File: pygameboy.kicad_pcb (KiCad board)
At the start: 2 copper layers, 49.3 x 59.7 mm, 93 parts, among them J1 Conn_01x01, J2 Conn_01x01, J3 Conn_ARM_JTAG_SWD_10, J4 USB_B_Micro, J5 MIDI IN, J6 MIDI OUT, Q1 BSS138, SW1 SW_Push, U1 CARTRIDGE, U2 SAMD51J, U3 74LVC244, U4 74LVC244, U5 74x4245, U6 74LVC244, U7 AP2204K-3.3, U8 H11L1

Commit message: Final v5 version
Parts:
- removed the G*** at (140.4, 46.0)
- added FID0: TestPoint, Fiducial:Fiducial_1mm_Mask2mm, F.Cu at (138.9, 82.5)
- added FID1: TestPoint, Fiducial:Fiducial_1mm_Mask2mm, F.Cu at (101.9, 55.0)
- added G***: LOGO, chickadee:chickadee_1mm_ss, F.Cu at (121.3, 44.9)
- added G***: Chickadee 3mm, chickadee:chickadee_3mm_fcu, B.Cu at (115.1, 45.8)
- added TP48: Test_Point, TestPoint:TestPoint_Pad_D1.5mm, B.Cu at (101.4, 95.5)
- added TP49: Test_Point, TestPoint:TestPoint_Pad_D1.5mm, B.Cu at (102.9, 92.5)
- added TP50: Test_Point, TestPoint:TestPoint_Pad_D1.5mm, B.Cu at (104.4, 95.5)
- added TP51: Test_Point, TestPoint:TestPoint_Pad_D1.5mm, B.Cu at (105.9, 92.5)
- added TP52: Test_Point, TestPoint:TestPoint_Pad_D1.5mm, B.Cu at (107.4, 95.5)
- added TP53: Test_Point, TestPoint:TestPoint_Pad_D1.5mm, B.Cu at (108.9, 92.5)
- added TP54: Test_Point, TestPoint:TestPoint_Pad_D1.5mm, B.Cu at (110.4, 95.5)
- added TP55: Test_Point, TestPoint:TestPoint_Pad_D1.5mm, B.Cu at (111.9, 92.5)
- added TP56: Test_Point, TestPoint:TestPoint_Pad_D1.5mm, B.Cu at (113.4, 95.5)
- added TP57: Test_Point, TestPoint:TestPoint_Pad_D1.5mm, B.Cu at (114.9, 92.5)
- added TP58: Test_Point, TestPoint:TestPoint_Pad_D1.5mm, B.Cu at (116.4, 95.5)
- added TP59: Test_Point, TestPoint:TestPoint_Pad_D1.5mm, B.Cu at (117.9, 92.5)
- added TP60: Test_Point, TestPoint:TestPoint_Pad_D1.5mm, B.Cu at (119.4, 95.5)
- added TP61: Test_Point, TestPoint:TestPoint_Pad_D1.5mm, B.Cu at (120.9, 92.5)
- added TP62: Test_Point, TestPoint:TestPoint_Pad_D1.5mm, B.Cu at (122.4, 95.5)
- added TP63: Test_Point, TestPoint:TestPoint_Pad_D1.5mm, B.Cu at (123.9, 92.5)
- added TP64: Test_Point, TestPoint:TestPoint_Pad_D1.5mm, B.Cu at (125.4, 95.5)
- added TP65: Test_Point, TestPoint:TestPoint_Pad_D1.5mm, B.Cu at (126.9, 92.5)
- added TP66: Test_Point, TestPoint:TestPoint_Pad_D1.5mm, B.Cu at (128.4, 95.5)
- added TP67: Test_Point, TestPoint:TestPoint_Pad_D1.5mm, B.Cu at (129.9, 92.5)
- added TP68: Test_Point, TestPoint:TestPoint_Pad_D1.5mm, B.Cu at (131.4, 95.5)
- added TP69: Test_Point, TestPoint:TestPoint_Pad_D1.5mm, B.Cu at (132.9, 92.5)
- added TP70: Test_Point, TestPoint:TestPoint_Pad_D1.5mm, B.Cu at (134.4, 95.5)
- added TP71: Test_Point, TestPoint:TestPoint_Pad_D1.5mm, B.Cu at (135.9, 92.5)
- added TP72: Test_Point, TestPoint:TestPoint_Pad_D1.5mm, B.Cu at (137.4, 95.5)
- added TP73: Test_Point, TestPoint:TestPoint_Pad_D1.5mm, B.Cu at (138.9, 92.5)
- added TP74: Test_Point, TestPoint:TestPoint_Pad_D1.5mm, B.Cu at (140.4, 95.5)
- added TP75: Test_Point, TestPoint:TestPoint_Pad_D1.5mm, B.Cu at (141.9, 92.5)
- added TP76: Test_Point, TestPoint:TestPoint_Pad_D1.5mm, B.Cu at (143.4, 95.4)
- added TP77: Test_Point, TestPoint:TestPoint_Pad_D1.5mm, B.Cu at (144.9, 92.5)
- added TP78: Test_Point, TestPoint:TestPoint_Pad_D1.5mm, B.Cu at (146.4, 95.5)
- added TP79: Test_Point, TestPoint:TestPoint_Pad_D1.5mm, B.Cu at (147.9, 92.5)
- added TP80: Test_Point, TestPoint:TestPoint_Pad_D1.5mm, B.Cu at (136.9, 43.0)
- added TP81: Test_Point, TestPoint:TestPoint_Pad_D1.5mm, B.Cu at (138.4, 45.5)
- added TP82: Test_Point, TestPoint:TestPoint_Pad_D1.5mm, B.Cu at (141.4, 45.5)
- added TP83: Test_Point, TestPoint:TestPoint_Pad_D1.5mm, B.Cu at (135.4, 45.5)
- added TP84: Test_Point, TestPoint:TestPoint_Pad_D1.5mm, B.Cu at (139.9, 43.0)
- added TP85: Test_Point, TestPoint:TestPoint_Pad_D1.5mm, B.Cu at (138.4, 41.0)
- moved R1 1.67 mm to (120.7, 50.5), turned to 270 degrees
- moved TP37 0.90 mm to (145.9, 50.2)
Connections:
- net Net-(TP31-Pad1) renamed /AUD
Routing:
- net /AUD: track 9.02 -> 19.0 mm
- net +BATT: track 19.0 -> 27.3 mm
- net /CS: track 13.8 -> 21.6 mm
- net /WR: track 16.9 -> 24.7 mm
- net /D5: track 45.1 -> 52.8 mm
- net /D3: track 44.4 -> 52.1 mm
- net /D1: track 45.2 -> 53.0 mm
- net /A7: track 18.1 -> 25.9 mm
- net /A5: track 14.4 -> 22.2 mm
- net /A3: track 12.6 -> 20.4 mm
- net /A15: track 13.1 -> 20.8 mm
- net /A11: track 17.6 -> 25.3 mm
- net /A1: track 17.0 -> 24.8 mm
- net /A9: track 12.6 -> 20.4 mm
- net /A13: track 13.9 -> 21.7 mm
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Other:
- outline, holes or cut-outs redrawn
- board text added: "+3V"
- board text added: "SWCLK"
- board text added: "SWDIO"
- board text added: "SWO"

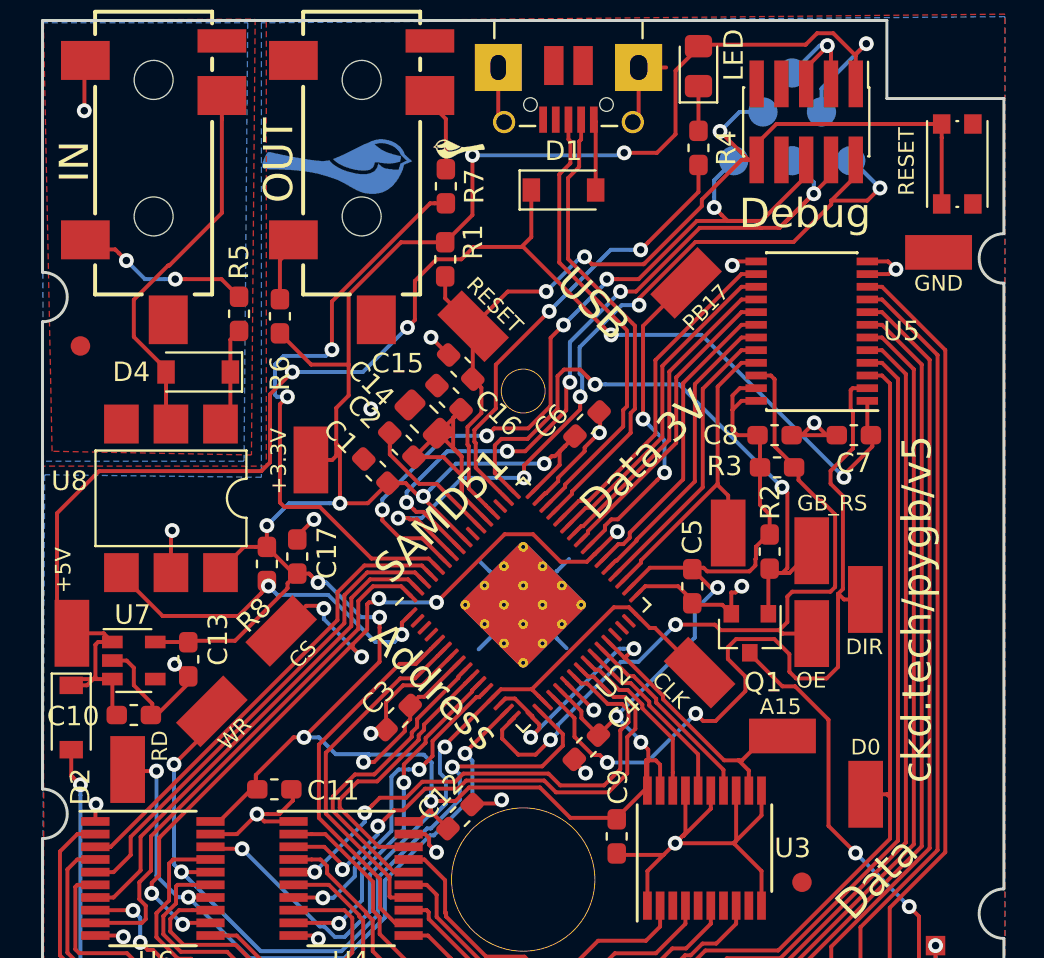
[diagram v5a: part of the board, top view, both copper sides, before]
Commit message: Correct optoistolator footprint. Tweak spacing.
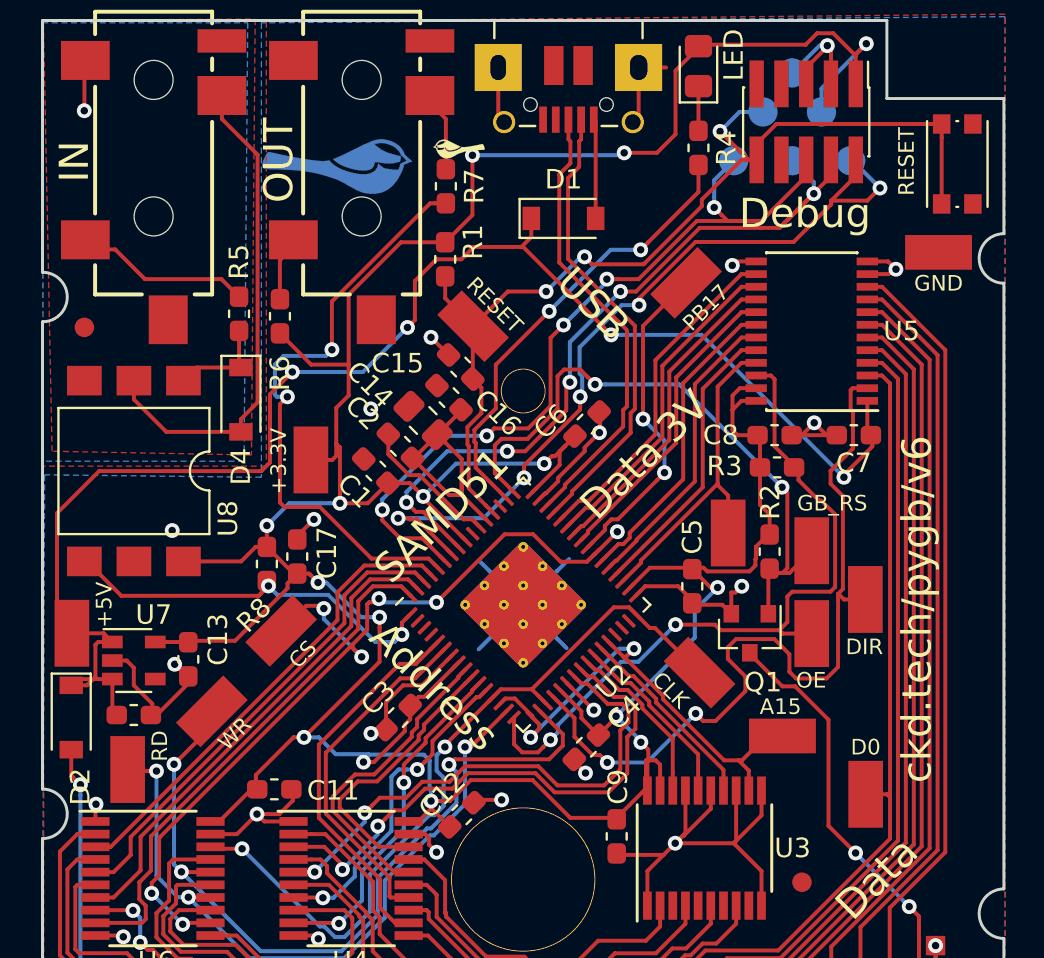
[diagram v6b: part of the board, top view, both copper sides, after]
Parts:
- TP33, TP34, TP35, TP36, TP37, TP38, TP39, TP40, TP41, TP42, TP43, TP44, TP45, TP46, TP47: footprint keystone:5015-SMT-TestPoint -> keystone:5015-SMT-TestPoint-NoPaste
- U8: footprint Package_DIP:SMDIP-6_W7.62mm -> Package_DIP:SMDIP-6_W9.53mm
- moved D4 2.61 mm to (110.2, 57.7), turned to 270 degrees
- moved U8 2.36 mm to (104.7, 61.4)
- moved D1 1.46 mm to (126.7, 48.4)
- moved FID1 0.97 mm to (102.1, 54.0)
- moved C12 0.13 mm to (121.5, 79.0)
- moved C2 0.10 mm to (118.4, 60.1)
- moved C14 0.09 mm to (119.5, 58.8)
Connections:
- J1 pad 1: Net-(J1-Pad1) -> (no net)
- J2 pad 1: Net-(J2-Pad1) -> (no net)
- J3 pad 7: Net-(J3-Pad7) -> (no net)
- J3 pad 8: Net-(J3-Pad8) -> (no net)
- J3 pad 9: Net-(J3-Pad9) -> (no net)
- J4 pad 4: Net-(J4-Pad4) -> (no net)
- J5 pad RN: Net-(J5-PadRN) -> (no net)
- J5 pad TN: Net-(J5-PadTN) -> (no net)
- J6 pad RN: Net-(J6-PadRN) -> (no net)
- J6 pad TN: Net-(J6-PadTN) -> (no net)
- U2 pad 2: Net-(U2-Pad2) -> (no net)
- U2 pad 29: Net-(U2-Pad29) -> (no net)
- U2 pad 3: Net-(U2-Pad3) -> (no net)
- U2 pad 30: Net-(U2-Pad30) -> (no net)
- U2 pad 31: Net-(U2-Pad31) -> (no net)
- U2 pad 4: Net-(U2-Pad4) -> (no net)
- U2 pad 51: Net-(U2-Pad51) -> (no net)
- U2 pad 55: Net-(U2-Pad55) -> (no net)
- U3 pad 3: Net-(U3-Pad3) -> (no net)
- U3 pad 5: Net-(U3-Pad5) -> (no net)
- U3 pad 7: Net-(U3-Pad7) -> (no net)
- U3 pad 9: Net-(U3-Pad9) -> (no net)
- U7 pad 4: Net-(U7-Pad4) -> (no net)
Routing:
- net Net-(D4-Pad2): track 19.5 -> 25.5 mm
- net Net-(C14-Pad2): track 15.6 -> 13.4 mm
- net GND: track 144.0 -> 142.1 mm
- net +3V3: track 196.0 -> 197.8 mm
- net +5V: track 78.8 -> 77.4 mm
- net VBUS: track 3.65 -> 5.10 mm
- net /MIDI_IN: track 18.6 -> 19.8 mm
- net /DATA_OE: track 38.5 -> 37.7 mm
- net Net-(J5-PadT): vias 2 -> 0
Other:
- board text added: "ckd.tech/pygb/v6"
- board text removed: "ckd.tech/pygb/v5"

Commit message: rp2040 start
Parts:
- removed G***: LOGO, chickadee:chickadee_1mm_ss
- removed G***: Chickadee 3mm, chickadee:chickadee_3mm_fcu
- removed TP38: 3.3v, keystone:5015-SMT-TestPoint-NoPaste
- removed TP44: PB17, keystone:5015-SMT-TestPoint-NoPaste
- added C18: 0.1uF, Capacitor_SMD:C_0603_1608Metric_Pad1.08x0.95mm_HandSolder, F.Cu at (118.4, 69.2)
- added C19: 1uF, Capacitor_SMD:C_0603_1608Metric_Pad1.08x0.95mm_HandSolder, F.Cu at (87.2, 45.6)
- added C20: 0.1uF, Capacitor_SMD:C_0603_1608Metric_Pad1.08x0.95mm_HandSolder, F.Cu at (91.5, 43.0)
- added C21: 0.1uF, Capacitor_SMD:C_0603_1608Metric_Pad1.08x0.95mm_HandSolder, F.Cu at (95.9, 40.5)
- added C22: 0.1uF, Capacitor_SMD:C_0603_1608Metric_Pad1.08x0.95mm_HandSolder, F.Cu at (126.9, 75.0)
- added R10: 1k, Resistor_SMD:R_0603_1608Metric_Pad0.98x0.95mm_HandSolder, F.Cu at (122.7, 76.2)
- added R11: 27, Resistor_SMD:R_0603_1608Metric_Pad0.98x0.95mm_HandSolder, F.Cu at (127.5, 59.5)
- added R12: 27, Resistor_SMD:R_0603_1608Metric_Pad0.98x0.95mm_HandSolder, F.Cu at (128.0, 61.5)
- added R9: 10k, Resistor_SMD:R_0603_1608Metric_Pad0.98x0.95mm_HandSolder, F.Cu at (118.3, 60.3)
- added U9: W25Q32JVSS, Package_SO:SOIC-8_5.23x5.23mm_P1.27mm, F.Cu at (118.4, 59.4)
- added Y1: 12mhz, Crystal:Crystal_SMD_Abracon_ABM3C-4Pin_5.0x3.2mm, F.Cu at (124.1, 77.6)
- C1, C2: value 0.1uF -> 22pF; footprint Capacitor_SMD:C_0603_1608Metric_Pad1.05x0.95mm_HandSolder -> Capacitor_SMD:C_0402_1005Metric_Pad0.74x0.62mm_HandSolder
- C10, C11, C12, C13, C16, C17, C3, C5, C6, C7, C8, C9: footprint Capacitor_SMD:C_0603_1608Metric_Pad1.05x0.95mm_HandSolder -> Capacitor_SMD:C_0603_1608Metric_Pad1.08x0.95mm_HandSolder
- C14: value 10uF -> 0.1uF; footprint Capacitor_SMD:C_0805_2012Metric_Pad1.15x1.40mm_HandSolder -> Capacitor_SMD:C_0603_1608Metric_Pad1.08x0.95mm_HandSolder
- C15: value 1uF -> 0.1uF; footprint Capacitor_SMD:C_0603_1608Metric_Pad1.05x0.95mm_HandSolder -> Capacitor_SMD:C_0603_1608Metric_Pad1.08x0.95mm_HandSolder
- C4: value 0.1uF -> 1uF; footprint Capacitor_SMD:C_0603_1608Metric_Pad1.05x0.95mm_HandSolder -> Capacitor_SMD:C_0603_1608Metric_Pad1.08x0.95mm_HandSolder
- R1, R2, R3, R4, R5, R6, R7, R8: footprint Resistor_SMD:R_0603_1608Metric_Pad1.05x0.95mm_HandSolder -> Resistor_SMD:R_0603_1608Metric_Pad0.98x0.95mm_HandSolder
- TP33, TP34, TP35, TP36, TP37, TP39, TP40, TP41, TP42, TP43, TP45, TP46, TP47: footprint keystone:5015-SMT-TestPoint-NoPaste -> keystone:5015-SMT-TestPoint
- U2: value SAMD51J -> RP2040; footprint Package_DFN_QFN:QFN-64-1EP_9x9mm_P0.5mm_EP4.7x4.7mm_ThermalVias -> MCU_RaspberryPi_and_Boards:RP2040-QFN-56
- moved C15 33.9 mm to (91.5, 40.5), turned to 0 degrees
- moved TP36 31.7 mm to (153.3, 48.3)
- moved C2 23.9 mm to (128.5, 81.7), turned to 0 degrees
- moved C1 21.9 mm to (125.3, 81.7), turned to 0 degrees
- moved C14 15.1 mm to (130.6, 69.1), turned to 0 degrees
- moved C3 14.7 mm to (124.3, 60.6), turned to 90 degrees
- moved C5 10.9 mm to (125.2, 74.6), turned to 270 degrees
- moved C16 6.07 mm to (124.0, 50.6)
- moved C4 4.55 mm to (123.5, 74.5), turned to 270 degrees
- moved C6 2.94 mm to (125.6, 60.8), turned to 90 degrees
- moved U2 0.06 mm to (124.6, 68.2), turned to 0 degrees
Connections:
- C1 pad 1: GND -> Net-(C1-Pad1)
- C1 pad 2: +3V3 -> GND
- C14 pad 1: GND -> +3V3
- C14 pad 2: Net-(C14-Pad2) -> GND
- C15 pad 1: GND -> +3V3
- C15 pad 2: Net-(C14-Pad2) -> GND
- C2 pad 1: Net-(C14-Pad2) -> Net-(C2-Pad1)
- C3 pad 1: GND -> Net-(C3-Pad1)
- C3 pad 2: +3V3 -> GND
- C4 pad 1: GND -> Net-(C3-Pad1)
- C4 pad 2: +3V3 -> GND
- C5 pad 1: GND -> Net-(C3-Pad1)
- C5 pad 2: +3V3 -> GND
- C6 pad 1: GND -> +3V3
- C6 pad 2: +3V3 -> GND
- J1 pad 1: (no net) -> Net-(J1-Pad1)
- J2 pad 1: (no net) -> Net-(J2-Pad1)
- J3 pad 6: /SWO -> Net-(J3-Pad6)
- J3 pad 7: (no net) -> Net-(J3-Pad7)
- J3 pad 8: (no net) -> Net-(J3-Pad8)
- J3 pad 9: (no net) -> Net-(J3-Pad9)
- J4 pad 4: (no net) -> Net-(J4-Pad4)
- J5 pad RN: (no net) -> Net-(J5-PadRN)
- J5 pad TN: (no net) -> Net-(J5-PadTN)
- J6 pad RN: (no net) -> /LED
- J6 pad TN: (no net) -> Net-(J6-PadTN)
- TP33 pad 1: /DIR -> /3V_RD
- U2 pad 1: /MIDI_IN -> +3V3
- U2 pad 10: /3V_A7 -> +3V3
- U2 pad 11: /3V_A8 -> /3V_A6
- U2 pad 12: /3V_A9 -> /3V_A7
- U2 pad 13: /3V_CLK -> /3V_A8
- U2 pad 14: /3V_A15 -> /3V_A9
- U2 pad 15: /3V_RD -> /3V_A10
- U2 pad 16: /DATA_OE -> /3V_A11
- U2 pad 17: /3V_A15 -> /3V_A12
- U2 pad 18: /3V_WR -> /3V_A13
- U2 pad 19: /3V_CLK -> GND
- U2 pad 2: (no net) -> /MIDI_OUT
- U2 pad 20: /DIR -> Net-(C1-Pad1)
- U2 pad 21: +3V3 -> Net-(R10-Pad1)
- U2 pad 22: GND -> +3V3
- U2 pad 23: /3V_A10 -> Net-(C3-Pad1)
- U2 pad 24: /3V_A11 -> /SWCLK
- U2 pad 25: /3V_A12 -> /SWDIO
- U2 pad 26: /3V_A13 -> /SAMD_RESET
- U2 pad 29: (no net) -> /3V_CLK
- U2 pad 3: (no net) -> /MIDI_IN
- U2 pad 30: (no net) -> /3V_RD
- U2 pad 31: (no net) -> /DATA_OE
- U2 pad 32: /3V_CLK -> /GB_RESET
- U2 pad 33: GND -> +3V3
- U2 pad 34: +3V3 -> /3V_D0
- U2 pad 35: /3V_D0 -> /3V_D1
- U2 pad 36: /3V_D1 -> /3V_D2
- U2 pad 37: /3V_D2 -> /3V_D3
- U2 pad 38: /3V_D3 -> /3V_D4
- U2 pad 39: /3V_CS -> /3V_D5
- U2 pad 4: (no net) -> /3V_A0
- U2 pad 40: Net-(TP44-Pad1) -> /3V_D6
- U2 pad 41: /3V_D4 -> /3V_D7
- U2 pad 42: /3V_D5 -> +3V3
- U2 pad 43: /3V_D6 -> +3V3
- U2 pad 44: /3V_D7 -> +3V3
- U2 pad 45: /USB_D- -> Net-(C3-Pad1)
- U2 pad 46: /USB_D+ -> Net-(R12-Pad1)
- U2 pad 47: GND -> Net-(R11-Pad1)
- U2 pad 49: /GB_RESET -> +3V3
- U2 pad 5: /3V_A4 -> /3V_A1
- U2 pad 50: /LED -> Net-(C3-Pad1)
- U2 pad 51: (no net) -> /QSPI_SD3
- U2 pad 52: /SAMD_RESET -> /QSPI_SCLK
- U2 pad 53: Net-(C14-Pad2) -> /QSPI_SD0
- U2 pad 54: GND -> /QSPI_SD2
- U2 pad 55: (no net) -> /QSPI_SD1
- U2 pad 56: +3V3 -> /QSPI_CS
- U2 pad 57: /SWCLK -> GND
- U2 pad 6: /3V_A5 -> /3V_A2
- U2 pad 7: GND -> /3V_A3
- U2 pad 8: +3V3 -> /3V_A4
- U2 pad 9: /3V_A6 -> /3V_A5
- U3 pad 3: (no net) -> Net-(U3-Pad3)
- U3 pad 5: (no net) -> Net-(U3-Pad5)
- U3 pad 7: (no net) -> Net-(U3-Pad7)
- U3 pad 9: (no net) -> Net-(U3-Pad9)
- U5 pad 2: /DIR -> /3V_RD
- U7 pad 4: (no net) -> Net-(U7-Pad4)
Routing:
- net /DIR: track 41.2 -> 0.00 mm, vias 2 -> 0
- net /3V_CS: track 45.8 -> 6.79 mm, vias 7 -> 2
- net GND: track 142.1 -> 105.2 mm, vias 24 -> 18
- net /3V_CLK: track 39.7 -> 3.25 mm, vias 2 -> 0
- net /SWDIO: track 42.6 -> 7.46 mm, vias 5 -> 1
- net +3V3: track 197.8 -> 162.8 mm, vias 15 -> 11
- net /SWO: track 42.2 -> 9.60 mm, vias 5 -> 1
- net /MIDI_OUT: track 31.0 -> 0.00 mm, vias 2 -> 0
- net /SWCLK: track 40.1 -> 9.24 mm, vias 5 -> 1
- net /3V_WR: track 41.4 -> 10.7 mm, vias 3 -> 2
- net /GB_RESET: track 32.7 -> 4.75 mm, vias 2 -> 0
- net /3V_A3: track 27.0 -> 0.00 mm
- net /3V_A2: track 25.3 -> 0.00 mm
- net /3V_A1: track 24.8 -> 0.00 mm
- net /3V_A0: track 24.2 -> 0.00 mm
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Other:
- board text added: "RP2040"
- board text removed: "SAMD51"

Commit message: More work on RP2350B
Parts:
- removed C12, C5, C9: 0.1uF, Capacitor_SMD:C_0603_1608Metric_Pad1.08x0.95mm_HandSolder
- removed C2: 22pF, Capacitor_SMD:C_0402_1005Metric_Pad0.74x0.62mm_HandSolder
- removed J3: Conn_ARM_JTAG_SWD_10, Pin_Headers:Pin_Header_Straight_2x05_Pitch1.27mm_SMD
- removed R11: 27, Resistor_SMD:R_0603_1608Metric_Pad0.98x0.95mm_HandSolder
- removed TP33: Test_Point, keystone:5015-SMT-TestPoint
- removed TP34: DATA_OE, keystone:5015-SMT-TestPoint
- removed TP35: GB_RESET, keystone:5015-SMT-TestPoint
- removed TP37: gnd, keystone:5015-SMT-TestPoint
- removed TP39: batt, keystone:5015-SMT-TestPoint
- removed TP40: clk, keystone:5015-SMT-TestPoint
- removed TP41: rd, keystone:5015-SMT-TestPoint
- removed TP42: wr, keystone:5015-SMT-TestPoint
- removed TP43: a15, keystone:5015-SMT-TestPoint
- removed TP45: cs, keystone:5015-SMT-TestPoint
- removed TP46: data0, keystone:5015-SMT-TestPoint
- removed TP47: D0, keystone:5015-SMT-TestPoint
- removed TP80, TP81, TP82, TP83, TP84, TP85: Test_Point, TestPoint:TestPoint_Pad_D1.5mm
- removed U3, U4, U6: 74LVC244, Package_SO:TSSOP-20_4.4x6.5mm_P0.65mm
- removed U9: W25Q32JVSS, Package_SO:SOIC-8_5.23x5.23mm_P1.27mm
- added C10: 4.7u, Capacitor_SMD:C_0402_1005Metric, F.Cu at (136.7, 72.9)
- added C13: 100n, Capacitor_SMD:C_0402_1005Metric, F.Cu at (134.0, 72.9)
- added C16: 100n, Capacitor_SMD:C_0402_1005Metric, F.Cu at (143.3, 65.1)
- added C17: 100n, Capacitor_SMD:C_0402_1005Metric, F.Cu at (127.3, 66.8)
- added C23: 100n, Capacitor_SMD:C_0402_1005Metric, F.Cu at (201.3, 40.5)
- added C24: 100n, Capacitor_SMD:C_0402_1005Metric, F.Cu at (201.3, 42.5)
- added C25: 100n, Capacitor_SMD:C_0402_1005Metric, F.Cu at (204.2, 38.6)
- added C26: 100n, Capacitor_SMD:C_0402_1005Metric, F.Cu at (204.2, 40.5)
- added C27: 100n, Capacitor_SMD:C_0402_1005Metric, F.Cu at (204.2, 42.5)
- added C7: 4.7u, RP2350_80QFN_minimal:C_0402_1005Metric_small_pads, F.Cu at (138.3, 57.6)
- added C8: 100n, Capacitor_SMD:C_0402_1005Metric, F.Cu at (127.3, 64.4)
- added L1: 3.3u, RP2350_80QFN_minimal:L_pol_2016, F.Cu at (197.9, 53.3)
- added R14: 1k, Resistor_SMD:R_0402_1005Metric, F.Cu at (195.6, 38.6)
- added R15: 33, Resistor_SMD:R_0402_1005Metric, F.Cu at (195.6, 40.6)
- added R16: 1k, Resistor_SMD:R_0402_1005Metric, F.Cu at (195.6, 42.6)
- added R17: 27, Resistor_SMD:R_0402_1005Metric, F.Cu at (195.6, 44.5)
- added R18: 27, Resistor_SMD:R_0402_1005Metric, F.Cu at (195.6, 46.5)
- added R2: 1k, Resistor_SMD:R_0402_1005Metric, F.Cu at (135.5, 72.9)
- added R3: 33, Resistor_SMD:R_0402_1005Metric, F.Cu at (140.5, 56.2)
- added R7: 27, Resistor_SMD:R_0402_1005Metric, F.Cu at (135.3, 55.8)
- added R8: 27, Resistor_SMD:R_0402_1005Metric, F.Cu at (136.3, 55.8)
- added U10: RP2350_80QFN, Package_DFN_QFN:QFN-80-1EP_10x10mm_P0.4mm_EP3.4x3.4mm_ThermalVias, F.Cu at (135.3, 64.6)
- C1: value 22pF -> 100n; footprint Capacitor_SMD:C_0402_1005Metric_Pad0.74x0.62mm_HandSolder -> Capacitor_SMD:C_0402_1005Metric
- C11, C18, C20, C21, C22: value 0.1uF -> 100n; footprint Capacitor_SMD:C_0603_1608Metric_Pad1.08x0.95mm_HandSolder -> Capacitor_SMD:C_0402_1005Metric
- C14, C15: value 0.1uF -> 4.7u; footprint Capacitor_SMD:C_0603_1608Metric_Pad1.08x0.95mm_HandSolder -> Capacitor_SMD:C_0402_1005Metric
- C19: value 1uF -> 100n; footprint Capacitor_SMD:C_0603_1608Metric_Pad1.08x0.95mm_HandSolder -> Capacitor_SMD:C_0402_1005Metric
- C3: value 0.1uF -> 15p; footprint Capacitor_SMD:C_0603_1608Metric_Pad1.08x0.95mm_HandSolder -> Capacitor_SMD:C_0402_1005Metric
- C4: value 1uF -> 15p; footprint Capacitor_SMD:C_0603_1608Metric_Pad1.08x0.95mm_HandSolder -> Capacitor_SMD:C_0402_1005Metric
- C6: value 0.1uF -> 4.7u; footprint Capacitor_SMD:C_0603_1608Metric_Pad1.08x0.95mm_HandSolder -> RP2350_80QFN_minimal:C_0402_1005Metric_small_pads
- J4: value USB_B_Micro -> USB_C_Receptacle_USB2.0_16P; footprint adafruit:4UCONN_20329_V2_USB -> Adafruit:USB_C_Receptacle_HRO_TYPE-C-31-M-31
- R10: value 1k -> 0; footprint Resistor_SMD:R_0603_1608Metric_Pad0.98x0.95mm_HandSolder -> Resistor_SMD:R_0402_1005Metric
- R12: value 27 -> DNF; footprint Resistor_SMD:R_0603_1608Metric_Pad0.98x0.95mm_HandSolder -> Resistor_SMD:R_0402_1005Metric
- R9: value 10k -> DNF; footprint Resistor_SMD:R_0603_1608Metric_Pad0.98x0.95mm_HandSolder -> Resistor_SMD:R_0402_1005Metric
- U2: value RP2040 -> W25Q128JVS; footprint MCU_RaspberryPi_and_Boards:RP2040-QFN-56 -> Package_SO:SOIC-8_5.3x5.3mm_P1.27mm
- Y1: value 12mhz -> ABM8-272-T3; footprint Crystal:Crystal_SMD_Abracon_ABM3C-4Pin_5.0x3.2mm -> Crystal:Crystal_SMD_3225-4Pin_3.2x2.5mm
- moved C20 111.8 mm to (202.4, 57.7)
- moved C19 111.3 mm to (198.5, 42.5)
- moved C21 98.4 mm to (190.2, 68.7), turned to 180 degrees
- moved C15 97.1 mm to (186.9, 59.1), turned to 180 degrees
- moved C11 92.4 mm to (202.9, 61.5)
- moved C1 84.9 mm to (198.5, 38.6)
- moved C18 84.1 mm to (202.4, 66.5), turned to 0 degrees
- moved C22 82.9 mm to (201.3, 38.6), turned to 0 degrees
- moved R10 78.5 mm to (192.7, 40.6)
- moved R9 77.5 mm to (192.7, 38.6)
- moved C4 73.1 mm to (196.5, 72.4), turned to 0 degrees
- moved C6 72.4 mm to (197.9, 55.9), turned to 0 degrees
- moved Y1 70.8 mm to (194.9, 76.0)
- moved C3 70.2 mm to (193.5, 72.4), turned to 180 degrees
- moved R12 66.8 mm to (192.7, 44.5)
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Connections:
- C1 pad 1: Net-(C1-Pad1) -> +3V3
- C11 pad 1: +3V3 -> +1V1
- C14 pad 1: +3V3 -> /RP2350 Core/VREG_AVDD
- C15 pad 1: +3V3 -> +1V1
- C18 pad 1: +3V3 -> +1V1
- C3 pad 1: Net-(C3-Pad1) -> /RP2350 Core/XIN
- C4 pad 1: Net-(C3-Pad1) -> Net-(C4-Pad1)
- C6 pad 1: +3V3 -> +1V1
- J1 pad 1: Net-(J1-Pad1) -> unconnected-(J1-Pin_1-Pad1)
- J2 pad 1: Net-(J2-Pad1) -> unconnected-(J2-Pin_1-Pad1)
- J5 pad RN: Net-(J5-PadRN) -> unconnected-(J5-PadRN)
- J5 pad TN: Net-(J5-PadTN) -> unconnected-(J5-PadTN)
- J6 pad TN: Net-(J6-PadTN) -> unconnected-(J6-PadTN)
- R10 pad 1: Net-(R10-Pad1) -> /RP2350 Core/QSPI_SS
- R10 pad 2: Net-(C2-Pad1) -> /RP2350 Core/FLASH_SS
- R12 pad 1: Net-(R12-Pad1) -> +3V3
- R12 pad 2: /USB_D- -> /RP2350 Core/FLASH_SS
- R9 pad 1: +3V3 -> /MIDI_OUT
- R9 pad 2: /QSPI_CS -> /RP2350 Core/FLASH_SS
- U2 pad 1: +3V3 -> /RP2350 Core/FLASH_SS
- U2 pad 2: /MIDI_OUT -> /RP2350 Core/QSPI_SD1
- U2 pad 3: /MIDI_IN -> /RP2350 Core/QSPI_SD2
- U2 pad 4: /3V_A0 -> GND
- U2 pad 5: /3V_A1 -> /RP2350 Core/QSPI_SD0
- U2 pad 6: /3V_A2 -> /RP2350 Core/QSPI_SCLK
- U2 pad 7: /3V_A3 -> /RP2350 Core/QSPI_SD3
- U2 pad 8: /3V_A4 -> +3V3
- U7 pad 4: Net-(U7-Pad4) -> unconnected-(U7-NC-Pad4)
- U8 pad 3: Net-(U8-Pad3) -> unconnected-(U8-Pad3)
- Y1 pad 1: Net-(C1-Pad1) -> /RP2350 Core/XIN
- Y1 pad 2: Net-(C2-Pad1) -> GND
- Y1 pad 3: (no net) -> Net-(C4-Pad1)
- Y1 pad 4: (no net) -> GND
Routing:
- net +3V3: track 162.8 -> 63.0 mm, vias 11 -> 1
- net GND: track 105.2 -> 43.8 mm, vias 18 -> 22
- net /D0: track 51.6 -> 12.2 mm
- net /D7: track 53.5 -> 14.4 mm
- net /D6: track 50.2 -> 11.5 mm
- net /D5: track 52.8 -> 14.5 mm
- net /D1: track 53.0 -> 15.2 mm
- net /D3: track 52.1 -> 14.5 mm
- net /D4: track 49.5 -> 12.4 mm
- net /SAMD_RESET: track 41.7 -> 5.88 mm, vias 3 -> 0
- net /D2: track 49.8 -> 14.4 mm
- net +1V1: track 0.00 -> 29.8 mm, vias 0 -> 6
- net /3V_A11: track 28.0 -> 0.00 mm, vias 2 -> 0
- net /3V_A10: track 26.8 -> 0.00 mm, vias 2 -> 0
- net +5V: track 77.4 -> 51.4 mm, vias 4 -> 2
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- added copper zone on F.Cu, net +1V1
- added copper zone on F.Cu, net +3V3
- added copper zone on F.Cu, net /RP2350 Core/VREG_LX
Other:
- net class Default removed
- rule pad_to_mask_clearance: 0.0508 -> 0.03
- board text added: "${REFERENCE}"
- board text added: "RP2350"
- board text added: "ckd.tech/pygb/v7"
- board text removed: "DIR"
- board text removed: "Data 3V"
- board text removed: "GB_RS"
- board text removed: "OE"
- board text removed: "PB17"
- board text removed: "RP2040"
- board text removed: "ckd.tech/pygb/v6"
